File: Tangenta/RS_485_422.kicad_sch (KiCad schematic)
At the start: 32 parts, among them J22 Conn_01x02_Pin, Q3 BSS138, U19 ADM2582E, U21 TPCDSOT23-SM712, U22 TPCDSOT23-SM712

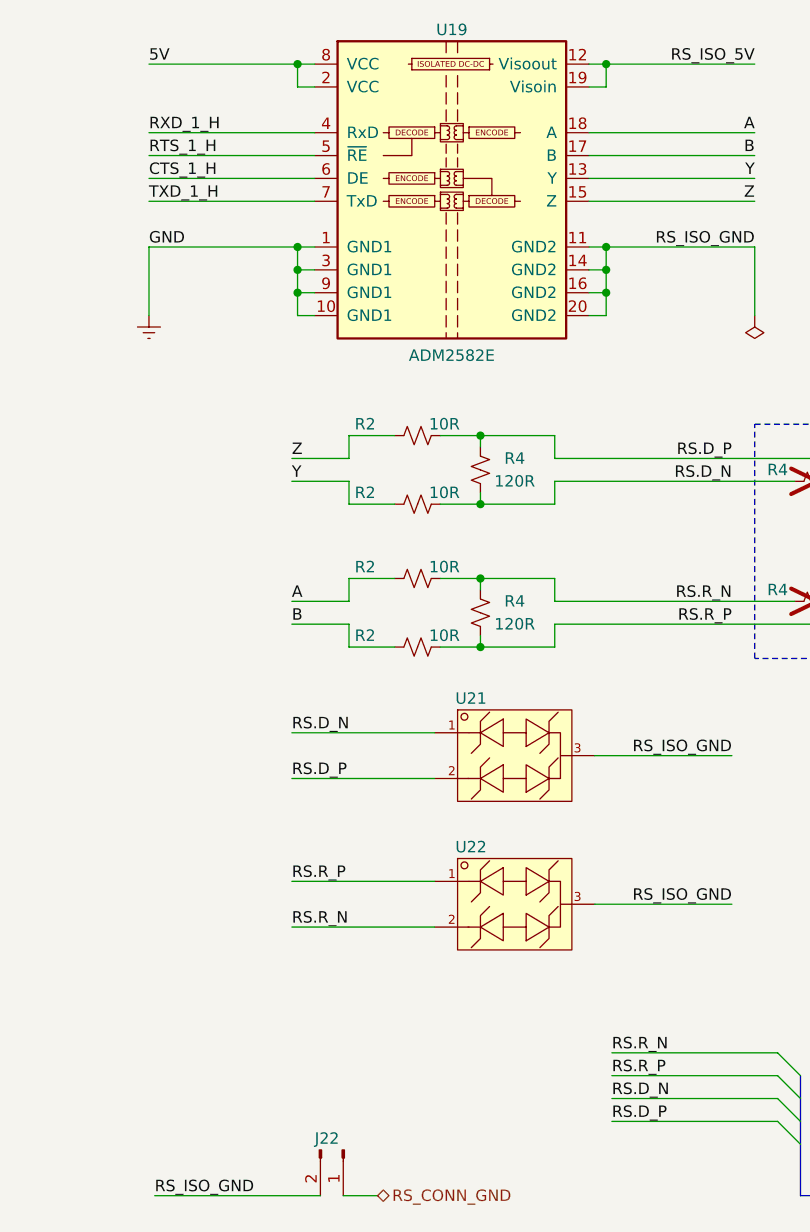
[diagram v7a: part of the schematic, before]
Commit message: Re-annotated. Ready for JLCPCB design verification.
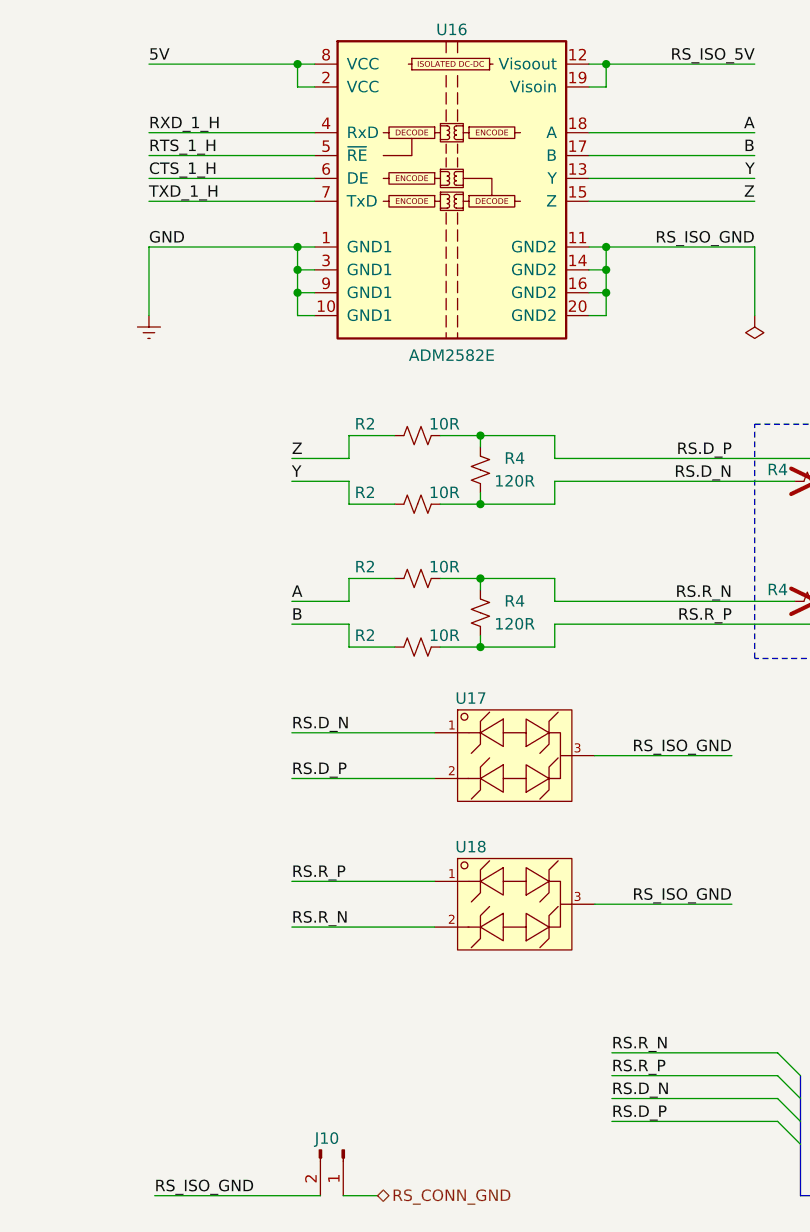
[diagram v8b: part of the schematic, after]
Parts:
- renumbered J22 to J10, U19 to U16, U21 to U17, U22 to U18
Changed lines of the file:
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@@
         )
         (path "/358d1bcf-7599-4352-8c4d-baa18a5f09e6/98e3b24f-9927-4339-b8fd-9deea91a522a"
-          (reference "R150") (unit 1)
+          (reference "R57") (unit 1)
         )
       )
@@
         )
         (path "/358d1bcf-7599-4352-8c4d-baa18a5f09e6/98e3b24f-9927-4339-b8fd-9deea91a522a"
-          (reference "R152") (unit 1)
+          (reference "R61") (unit 1)
         )
       )
@@
         )
         (path "/358d1bcf-7599-4352-8c4d-baa18a5f09e6/98e3b24f-9927-4339-b8fd-9deea91a522a"
-          (reference "R171") (unit 1)
+          (reference "R67") (unit 1)
         )
       )
@@
         )
         (path "/358d1bcf-7599-4352-8c4d-baa18a5f09e6/98e3b24f-9927-4339-b8fd-9deea91a522a"
-          (reference "R157") (unit 1)
+          (reference "R59") (unit 1)
         )
       )
@@
         )
         (path "/358d1bcf-7599-4352-8c4d-baa18a5f09e6/98e3b24f-9927-4339-b8fd-9deea91a522a"
-          (reference "R169") (unit 1)
+          (reference "R63") (unit 1)
         )
       )
@@
         )
         (path "/358d1bcf-7599-4352-8c4d-baa18a5f09e6/98e3b24f-9927-4339-b8fd-9deea91a522a"
-          (reference "R182") (unit 1)
+          (reference "R65") (unit 1)
         )
       )
@@
         )
         (path "/358d1bcf-7599-4352-8c4d-baa18a5f09e6/98e3b24f-9927-4339-b8fd-9deea91a522a"
-          (reference "C181") (unit 1)
+          (reference "C101") (unit 1)
         )
       )
@@
         )
         (path "/358d1bcf-7599-4352-8c4d-baa18a5f09e6/98e3b24f-9927-4339-b8fd-9deea91a522a"
-          (reference "Q8") (unit 1)
+          (reference "Q6") (unit 1)
         )
       )
@@
         )
         (path "/358d1bcf-7599-4352-8c4d-baa18a5f09e6/98e3b24f-9927-4339-b8fd-9deea91a522a"
-          (reference "R170") (unit 1)
+          (reference "R64") (unit 1)
         )
       )
@@
         )
         (path "/358d1bcf-7599-4352-8c4d-baa18a5f09e6/98e3b24f-9927-4339-b8fd-9deea91a522a"
-          (reference "R173") (unit 1)
+          (reference "R69") (unit 1)
         )
       )
@@
         )
         (path "/358d1bcf-7599-4352-8c4d-baa18a5f09e6/98e3b24f-9927-4339-b8fd-9deea91a522a"
-          (reference "C183") (unit 1)
+          (reference "C102") (unit 1)
         )
       )
@@
         )
         (path "/358d1bcf-7599-4352-8c4d-baa18a5f09e6/98e3b24f-9927-4339-b8fd-9deea91a522a"
-          (reference "#PWR076") (unit 1)
+          (reference "#PWR055") (unit 1)
         )
       )
@@
         )
         (path "/358d1bcf-7599-4352-8c4d-baa18a5f09e6/98e3b24f-9927-4339-b8fd-9deea91a522a"
-          (reference "R153") (unit 1)
+          (reference "R62") (unit 1)
         )
       )
@@
         )
         (path "/358d1bcf-7599-4352-8c4d-baa18a5f09e6/98e3b24f-9927-4339-b8fd-9deea91a522a"
-          (reference "C180") (unit 1)
+          (reference "C99") (unit 1)
         )
       )
@@
         )
         (path "/358d1bcf-7599-4352-8c4d-baa18a5f09e6/98e3b24f-9927-4339-b8fd-9deea91a522a"
-          (reference "#PWR079") (unit 1)
+          (reference "#PWR057") (unit 1)
         )
       )
@@
         )
         (path "/358d1bcf-7599-4352-8c4d-baa18a5f09e6/98e3b24f-9927-4339-b8fd-9deea91a522a"
-          (reference "R155") (unit 1)
+          (reference "R58") (unit 1)
         )
       )
@@
         )
         (path "/358d1bcf-7599-4352-8c4d-baa18a5f09e6/98e3b24f-9927-4339-b8fd-9deea91a522a"
-          (reference "Q7") (unit 1)
+          (reference "Q5") (unit 1)
         )
       )
@@
         )
         (path "/358d1bcf-7599-4352-8c4d-baa18a5f09e6/98e3b24f-9927-4339-b8fd-9deea91a522a"
-          (reference "C184") (unit 1)
+          (reference "C98") (unit 1)
         )
       )
@@
         )
         (path "/358d1bcf-7599-4352-8c4d-baa18a5f09e6/98e3b24f-9927-4339-b8fd-9deea91a522a"
-          (reference "R156") (unit 1)
+          (reference "R55") (unit 1)
         )
       )
@@
         )
         (path "/358d1bcf-7599-4352-8c4d-baa18a5f09e6/98e3b24f-9927-4339-b8fd-9deea91a522a"
-          (reference "R158") (unit 1)
+          (reference "R56") (unit 1)
         )
       )
@@
   (symbol (lib_id "CholaSymbolsPrjLib:TPCDSOT23-SM712") (at 216.916 127.635 0) (unit 1)
     (in_bom yes) (on_board yes) (dnp no)
-    (property "Reference" "U22" (at 210.566 121.285 0)
+    (property "Reference" "U18" (at 210.566 121.285 0)
       (effects (font (size 1.27 1.27)) (justify left))
     )
@@
       (project "Tangenta"
         (path "/358d1bcf-7599-4352-8c4d-baa18a5f09e6/98e3b24f-9927-4339-b8fd-9deea91a522a"
-          (reference "U22") (unit 1)
+          (reference "U18") (unit 1)
         )
       )
@@
         )
         (path "/358d1bcf-7599-4352-8c4d-baa18a5f09e6/98e3b24f-9927-4339-b8fd-9deea91a522a"
-          (reference "R149") (unit 1)
+          (reference "R53") (unit 1)
         )
       )
@@
         )
         (path "/358d1bcf-7599-4352-8c4d-baa18a5f09e6/98e3b24f-9927-4339-b8fd-9deea91a522a"
-          (reference "C186") (unit 1)
+          (reference "C104") (unit 1)
         )
       )
@@
         )
         (path "/358d1bcf-7599-4352-8c4d-baa18a5f09e6/98e3b24f-9927-4339-b8fd-9deea91a522a"
-          (reference "#PWR081") (unit 1)
+          (reference "#PWR056") (unit 1)
         )
       )
@@
         )
         (path "/358d1bcf-7599-4352-8c4d-baa18a5f09e6/98e3b24f-9927-4339-b8fd-9deea91a522a"
-          (reference "Q9") (unit 1)
+          (reference "Q7") (unit 1)
         )
       )
@@
   (symbol (lib_id "CholaSymbolsPrjLib:ADM2582E") (at 210.185 49.53 0) (unit 1)
     (in_bom yes) (on_board yes) (dnp no)
-    (property "Reference" "U19" (at 210.185 30.48 0)
+    (property "Reference" "U16" (at 210.185 30.48 0)
       (effects (font (size 1.27 1.27)))
     )
@@
       (project "Tangenta"
         (path "/358d1bcf-7599-4352-8c4d-baa18a5f09e6/98e3b24f-9927-4339-b8fd-9deea91a522a"
-          (reference "U19") (unit 1)
+          (reference "U16") (unit 1)
         )
       )
@@
         )
         (path "/358d1bcf-7599-4352-8c4d-baa18a5f09e6/98e3b24f-9927-4339-b8fd-9deea91a522a"
-          (reference "R159") (unit 1)
+          (reference "R60") (unit 1)
         )
       )
@@
         )
         (path "/358d1bcf-7599-4352-8c4d-baa18a5f09e6/98e3b24f-9927-4339-b8fd-9deea91a522a"
-          (reference "Q10") (unit 1)
+          (reference "Q8") (unit 1)
         )
       )
@@
         )
         (path "/358d1bcf-7599-4352-8c4d-baa18a5f09e6/98e3b24f-9927-4339-b8fd-9deea91a522a"
-          (reference "C185") (unit 1)
+          (reference "C103") (unit 1)
         )
       )
@@
         )
         (path "/358d1bcf-7599-4352-8c4d-baa18a5f09e6/98e3b24f-9927-4339-b8fd-9deea91a522a"
-          (reference "R154") (unit 1)
+          (reference "R54") (unit 1)
         )
       )
@@
         )
         (path "/358d1bcf-7599-4352-8c4d-baa18a5f09e6/98e3b24f-9927-4339-b8fd-9deea91a522a"
-          (reference "R172") (unit 1)
+          (reference "R68") (unit 1)
         )
       )
@@
   (symbol (lib_id "CholaSymbolsPrjLib:Conn_01x02_Pin") (at 198.12 154.94 270) (unit 1)
     (in_bom yes) (on_board yes) (dnp no)
-    (property "Reference" "J22" (at 194.945 153.67 90)
+    (property "Reference" "J10" (at 194.945 153.67 90)
       (effects (font (size 1.27 1.27)) (justify left))
     )
@@
       (project "Tangenta"
         (path "/358d1bcf-7599-4352-8c4d-baa18a5f09e6/98e3b24f-9927-4339-b8fd-9deea91a522a"
-          (reference "J22") (unit 1)
+          (reference "J10") (unit 1)
         )
       )
@@
         )
         (path "/358d1bcf-7599-4352-8c4d-baa18a5f09e6/98e3b24f-9927-4339-b8fd-9deea91a522a"
-          (reference "R183") (unit 1)
+          (reference "R66") (unit 1)
         )
       )
@@
   (symbol (lib_id "CholaSymbolsPrjLib:TPCDSOT23-SM712") (at 216.916 111.125 0) (unit 1)
     (in_bom yes) (on_board yes) (dnp no)
-    (property "Reference" "U21" (at 210.566 104.775 0)
+    (property "Reference" "U17" (at 210.566 104.775 0)
       (effects (font (size 1.27 1.27)) (justify left))
     )
@@
       (project "Tangenta"
         (path "/358d1bcf-7599-4352-8c4d-baa18a5f09e6/98e3b24f-9927-4339-b8fd-9deea91a522a"
-          (reference "U21") (unit 1)
+          (reference "U17") (unit 1)
         )
       )
@@
         )
         (path "/358d1bcf-7599-4352-8c4d-baa18a5f09e6/98e3b24f-9927-4339-b8fd-9deea91a522a"
-          (reference "C182") (unit 1)
+          (reference "C100") (unit 1)
         )
       )
@@
         )
         (path "/358d1bcf-7599-4352-8c4d-baa18a5f09e6/98e3b24f-9927-4339-b8fd-9deea91a522a"
-          (reference "#PWR078") (unit 1)
-        )
-      )
+          (reference "#PWR058") (unit 1)
+        )
+      )
